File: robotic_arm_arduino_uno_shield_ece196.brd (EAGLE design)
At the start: 53.3 x 53.3 mm, 37 parts, among them J1 (ID,OD)=(2.1,5.5)MM

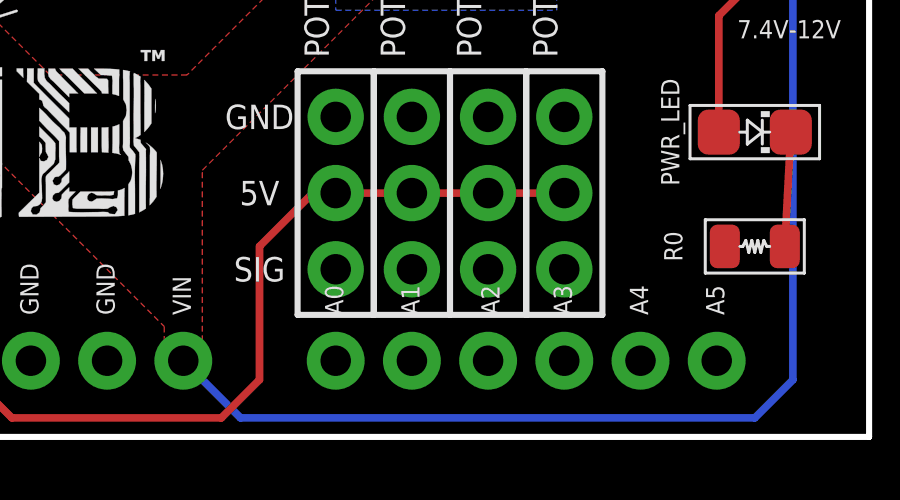
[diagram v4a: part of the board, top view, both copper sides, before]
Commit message: Rev 4: Fixed error not connecting analog pins.  Ready for fab.
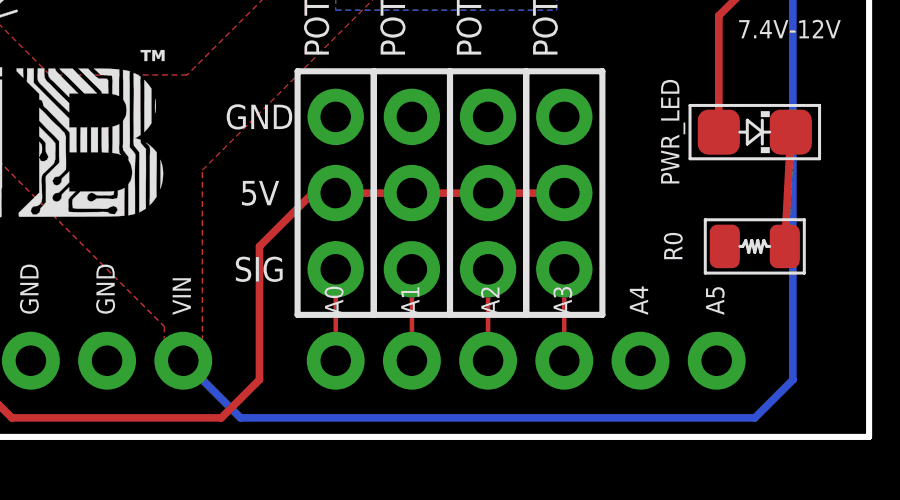
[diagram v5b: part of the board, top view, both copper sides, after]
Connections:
- net N$33 renamed A4
- net N$34 renamed A5
- removed net N$29: ARDUINO1.A0
- removed net N$30: ARDUINO1.A1
- removed net N$31: ARDUINO1.A2
- removed net N$32: ARDUINO1.A3
- net A0: now also ARDUINO1.A0
- net A1: now also ARDUINO1.A1
- net A2: now also ARDUINO1.A2
- net A3: now also ARDUINO1.A3
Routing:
- net A3: track 0.00 -> 3.05 mm
- net A2: track 0.00 -> 3.05 mm
- net A1: track 0.00 -> 3.05 mm
- net A0: track 0.00 -> 3.05 mm
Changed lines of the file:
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@@
 <element name="ARDUINO1" library="PiB_boards" package="ARDUINO_UNO_R3_NO-HOLES_NO-AVR-ISP_NO-I2C_NO-NC_NO-IOREF" value="Arduino UNO R3" x="44.45" y="0" rot="R90">
 <attribute name="DATASHEET" value="https://media.digikey.com/pdf/Data%20Sheets/Arduino%20PDFs/A000066_Web.pdf" x="44.45" y="0" size="1.778" layer="27" rot="R90" display="off"/>
+<attribute name="DATASHEET_CONNECTOR" value="http://www.sullinscorp.com/drawings/77____C___S___N-OMIT,_M500,_STRAIGHT,_C10436.pdf" x="44.45" y="0" size="1.778" layer="27" rot="R90" display="off"/>
 <attribute name="DIST" value="Digikey" x="44.45" y="0" size="1.778" layer="27" rot="R90" display="off"/>
 <attribute name="DISTLINK" value="https://www.digikey.com/products/en?keywords=1050-1024-ND" x="44.45" y="0" size="1.778" layer="27" rot="R90" display="off"/>
+<attribute name="DISTLINK_CONNECTOR1" value="https://www.digikey.com/products/en?keywords=S1012E-06-ND" x="44.45" y="0" size="1.778" layer="27" rot="R90" display="off"/>
+<attribute name="DISTLINK_CONNECTOR2" value="https://www.digikey.com/products/en?keywords=PEC08SAAN" x="44.45" y="0" size="1.778" layer="27" rot="R90" display="off"/>
 <attribute name="DISTPN" value="1050-1024-ND" x="44.45" y="0" size="1.778" layer="27" rot="R90" display="off"/>
+<attribute name="DISTPN_CONNECTOR1" value="S1012E-06-ND" x="44.45" y="0" size="1.778" layer="27" rot="R90" display="off"/>
+<attribute name="DISTPN_CONNECTOR2" value="S1012E-08-ND" x="44.45" y="0" size="1.778" layer="27" rot="R90" display="off"/>
+<attribute name="DIST_CONNECTOR" value="Digikey" x="44.45" y="0" size="1.778" layer="27" rot="R90" display="off"/>
 <attribute name="MFR" value="Arduino" x="44.45" y="0" size="1.778" layer="27" rot="R90" display="off"/>
+<attribute name="MFR_CONNECTOR" value="Sullins Connector Solutions" x="44.45" y="0" size="1.778" layer="27" rot="R90" display="off"/>
 <attribute name="MPN" value="A000066" x="44.45" y="0" size="1.778" layer="27" rot="R90" display="off"/>
+<attribute name="MPN_CONNECTOR1" value="PEC06SAAN" x="44.45" y="0" size="1.778" layer="27" rot="R90" display="off"/>
+<attribute name="MPN_CONNECTOR2" value="PEC08SAAN" x="44.45" y="0" size="1.778" layer="27" rot="R90" display="off"/>
+<attribute name="QTY_CONNECTOR1" value="2" x="44.45" y="0" size="1.778" layer="27" rot="R90" display="off"/>
+<attribute name="QTY_CONNECTOR2" value="2" x="44.45" y="0" size="1.778" layer="27" rot="R90" display="off"/>
 </element>
 </elements>
@@
 <signal name="A0">
 <contactref element="POT1" pad="S"/>
+<contactref element="ARDUINO1" pad="A0"/>
+<wire x1="29.21" y1="5.588" x2="29.21" y2="2.54" width="0.1524" layer="1"/>
 </signal>
 <signal name="A1">
 <contactref element="POT2" pad="S"/>
+<contactref element="ARDUINO1" pad="A1"/>
+<wire x1="31.75" y1="2.54" x2="31.75" y2="5.588" width="0.1524" layer="1"/>
 </signal>
 <signal name="A2">
 <contactref element="POT3" pad="S"/>
+<contactref element="ARDUINO1" pad="A2"/>
+<wire x1="34.29" y1="2.54" x2="34.29" y2="5.588" width="0.1524" layer="1"/>
 </signal>
 <signal name="A3">
 <contactref element="POT4" pad="S"/>
+<contactref element="ARDUINO1" pad="A3"/>
+<wire x1="36.83" y1="5.588" x2="36.83" y2="2.54" width="0.1524" layer="1"/>
 </signal>
 <signal name="VIN">
@@
 <contactref element="SERVO4" pad="3"/>
 </signal>
-<signal name="N$29">
-<contactref element="ARDUINO1" pad="A0"/>
-</signal>
-<signal name="N$30">
-<contactref element="ARDUINO1" pad="A1"/>
-</signal>
-<signal name="N$31">
-<contactref element="ARDUINO1" pad="A2"/>
-</signal>
-<signal name="N$32">
-<contactref element="ARDUINO1" pad="A3"/>
-</signal>
-<signal name="N$33">
+<signal name="A4">
 <contactref element="ARDUINO1" pad="A4"/>
 </signal>
-<signal name="N$34">
+<signal name="A5">
 <contactref element="ARDUINO1" pad="A5"/>
 </signal>
